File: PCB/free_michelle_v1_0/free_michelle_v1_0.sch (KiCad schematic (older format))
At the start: 100 parts, among them J1 Zworka_TX, J10 ARK, J11 ARK, J12 Zworka_Buzzer, J13 ARK, J14 ARK, J15 Gniazdo 5VP DC 5,5x2,5, J16 Gniazdo 9V DC 5,5x2,5, J2 Zworka_RX, J3 GROVE_SW, J4 ARK, J5 ARK, J6 ARK, J7 ARK, J8 GROVE_SW, J9 A02YYUW_GroveCON, K1 FINDER-36.11, K2 FINDER-36.11, K3 FINDER-36.11, K4 FINDER-36.11, K5 FINDER-36.11, K6 FINDER-36.11, K7 FINDER-36.11, K8 FINDER-36.11, Q1 MMBT4403_PNP, Q2 MMBT4403_PNP, Q3 MMBT4403_PNP, Q4 MMBT4403_PNP, Q5 BSS138, Q6 MMBT4403_PNP, Q7 MMBT4403_PNP, Q8 MMBT4403_PNP, Q9 MMBT4403_PNP, SW1 Rotary_Encoder, SW2 SW_Push, SW3 SW_Push, U1 EEPROM_24AA01, U2 ESP8266_NodeMCU_v2, U3 DS3231M_RTC, U4 NRF24L01_Breakout, U5 BMP280, U6 LD1117V33, U7 L7805, U8 LD1117V33

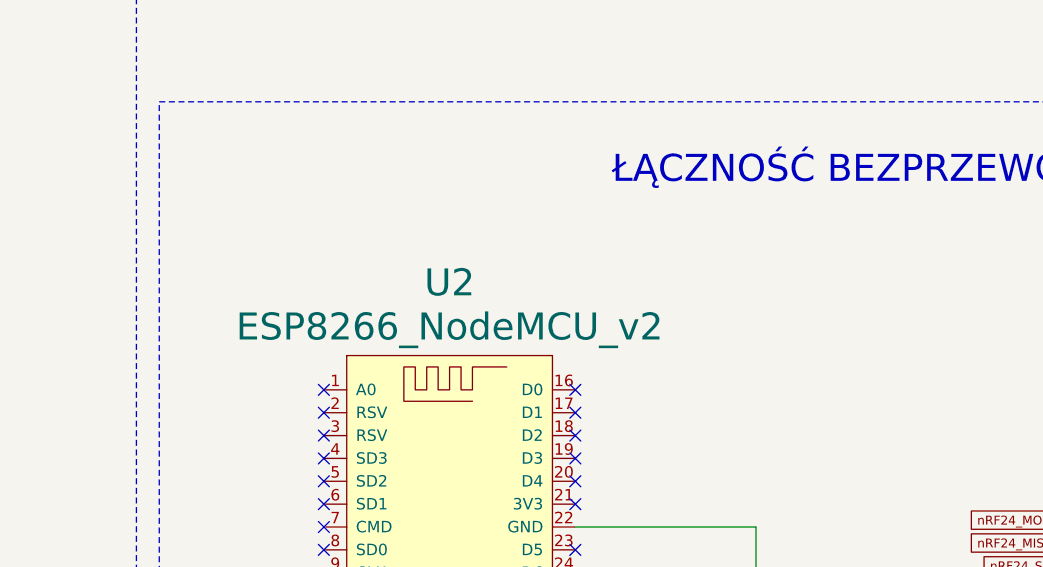
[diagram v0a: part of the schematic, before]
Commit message: Powybierane wszystkie obudowy i poprzypisywane footprinty
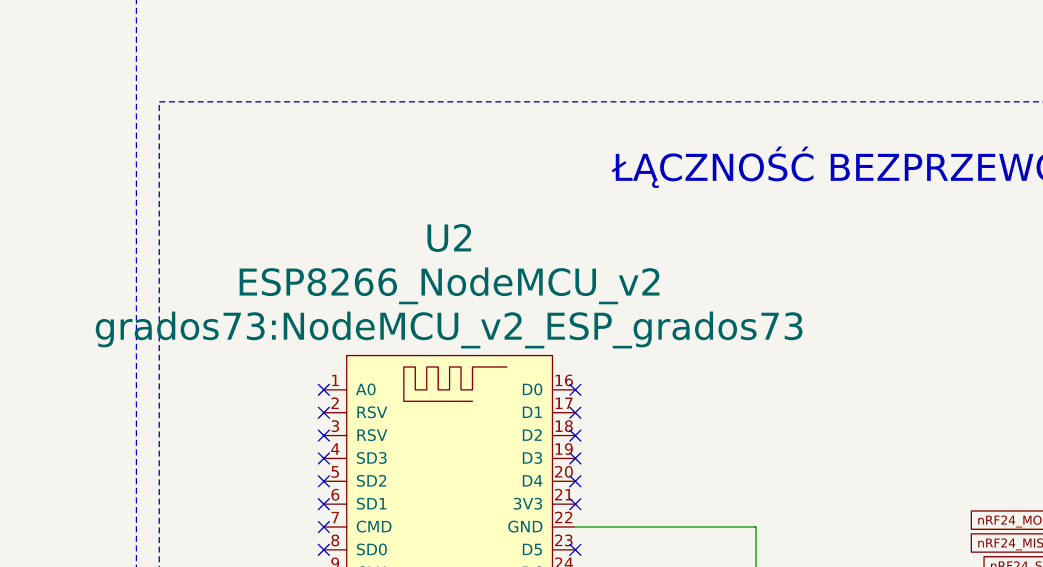
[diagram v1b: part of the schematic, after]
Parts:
- C1, C2, C3, C4, C6, C7, C8: footprint (none) -> Capacitor_SMD:C_1206_3216Metric
- C10, C12, C13, C15, C16, C17: footprint (none) -> Capacitor_THT:C_Disc_D5.0mm_W2.5mm_P5.00mm
- C11, C14, C9: footprint (none) -> Capacitor_THT:CP_Radial_D5.0mm_P2.50mm
- C5: footprint (none) -> Capacitor_THT:C_Disc_D3.0mm_W2.0mm_P2.50mm
- D1: footprint (none) -> grados73:TFT_2_4_c_240x320_SPI
- D10, D3, D4, D5, D6, D7, D8, D9: footprint (none) -> Diode_THT:D_DO-41_SOD81_P10.16mm_Horizontal
- D11: footprint LED_THT:LED_D3.0mm_Clear -> LED_THT:LED_D3.0mm
- D12: footprint (none) -> LED_THT:LED_D3.0mm_Clear
- J10, J11, J13, J14, J4, J5, J6, J7: footprint (none) -> TerminalBlock:TerminalBlock_Altech_AK300-3_P5.00mm
- J15: footprint (none) -> TerminalBlock:TerminalBlock_Altech_AK300-2_P5.00mm
- J16: footprint (none) -> Connector_BarrelJack:BarrelJack_Horizontal
- R1, R10, R11, R12, R13, R14, R15, R16, R17, R18, R19, R2, R3, R4, R5, R6, R7, R9: footprint (none) -> Resistor_SMD:R_1206_3216Metric
- R20, R21, R8: footprint (none) -> Resistor_THT:R_Axial_DIN0207_L6.3mm_D2.5mm_P7.62mm_Horizontal
- U2: footprint (none) -> grados73:NodeMCU_v2_ESP_grados73

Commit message: Ulozone wstepnie elementy na PCB
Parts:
- Term1: footprint Connector_PinHeader_2.00mm:PinHeader_1x04_P2.00mm_Vertical -> Connector_PinHeader_2.00mm:PinHeader_1x04_P2.00mm_Horizontal
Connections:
- net +5VP: now also D12.2 (A), SW3.1; no longer R21.1
- net +9V: now also D11.2 (A), SW2.1; no longer R20.1
- net DS3231_SCL_PB6: no longer R2.1
- net DS3231_SDA_PB9: now also R2.1
- net ESP_TX_RX_STM__U1_PB7: now also J1.2 (Pin_2)
- net GND: now also R20.1, R21.1, U2.22 (GND)
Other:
- note removed: "LOGIKI 3,3V"
- note removed: "LOGIKI 5V"
- note removed: "NAPIĘCIE ZASILANIA 3,3V"
- moved on the sheet: D11, D12, J15, J16, R20, R21, SW2, SW3

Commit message: Poprawki po rozmowie z Mackiem umieszczone na schemacie
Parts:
- removed LED1: WS2812b_ARK, Connector_PinHeader_2.54mm:PinHeader_1x03_P2.54mm_Vertical, symbol Connector:Conn_01x03_Female
- added LED1: WS2812b_GROVE, Connector_PinHeader_2.00mm:PinHeader_1x04_P2.00mm_Horizontal, symbol Connector:Conn_01x04_Male
- added R22: 4K7, Resistor_SMD:R_1206_3216Metric, symbol Device:R_Small
- C7, C8: footprint Capacitor_SMD:C_1206_3216Metric -> Capacitor_THT:C_Disc_D5.0mm_W2.5mm_P2.50mm
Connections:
- net +3V3: now also J3.4 (Pin_4), J8.4 (Pin_4), Term1.4 (Pin_4), R22.1; no longer J3.1 (Pin_1), J8.1 (Pin_1)
- net +5V: no longer C7.1, C8.1, Term1.4 (Pin_4)
- net +5VP: now also C7.1, LED1.4 (Pin_4)
- net +9V: now also C8.1
- net DS18B20_1WIRE_PA15: now also R22.2
- net GND: now also J3.2 (Pin_2), J8.2 (Pin_2), LED1.2 (Pin_2); no longer J3.4 (Pin_4), J8.4 (Pin_4)
- net at TFT_CONTROLLER1.42 (SWCLK): now also J3.1 (Pin_1); no longer J3.3 (Pin_3)
- net at TFT_CONTROLLER1.43 (SWIO): now also J3.3 (Pin_3); no longer J3.2 (Pin_2)
- net at GPIO_CONTROLLER1.42 (SWCLK): now also J8.1 (Pin_1); no longer J8.3 (Pin_3)
- net at GPIO_CONTROLLER1.43 (SWIO): now also J8.3 (Pin_3); no longer J8.2 (Pin_2)
- net at Q5.3 (D), R15.1: now also LED1.3 (Pin_3)
- no-connect marks 56 -> 57

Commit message: Gotowa płytka przed generacją gerberow
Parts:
- removed U6, U8: LD1117V33, Package_TO_SOT_THT:TO-220-3_Vertical, symbol grad73_library:LD1117V33
- added H1, H2, H3, H4: MountingHole, MountingHole:MountingHole_3.2mm_M3, symbol Mechanical:MountingHole
- added U6, U8: LD1117AV33, Package_TO_SOT_THT:TO-220-3_Vertical, symbol Regulator_Linear:LD1117S12TR_SOT223
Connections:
- net +3.3VP: now also U6.2 (VO)
- net +3V3: now also U8.2 (VO)
- net +9V: now also U6.3 (VI), U8.3 (VI)
- net GND: now also U6.1 (GND), U8.1 (GND)
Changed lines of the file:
@@
 	19610 4090 19450 4090
-$Comp
-L grad73_library:LD1117V33 U8
-U 1 1 61E4A9E3
-P 20120 2810
-F 0 "U8" H 20120 3052 50  0000 C CNN
-F 1 "LD1117V33" H 20120 2961 50  0000 C CNN
-F 2 "Package_TO_SOT_THT:TO-220-3_Vertical" H 20145 2660 50  0001 L CIN
-F 3 "" H 20120 2760 50  0001 C CNN
-	1    20120 2810
-	1    0    0    -1
-$EndComp
 $Comp
 L free_michelle_v1_0-rescue:grad73_library_24AA01-free_michelle_v1_0-cache U1
@@
 NoConn ~ 12380 4120
 $Comp
-L grad73_library:LD1117V33 U6
-U 1 1 64E78405
-P 17820 2830
-F 0 "U6" H 17820 3072 50  0000 C CNN
-F 1 "LD1117V33" H 17820 2981 50  0000 C CNN
-F 2 "Package_TO_SOT_THT:TO-220-3_Vertical" H 17845 2680 50  0001 L CIN
-F 3 "" H 17820 2780 50  0001 C CNN
-	1    17820 2830
-	1    0    0    -1
-$EndComp
-$Comp
 L power:+9V #PWR045
 U 1 1 64E7923F
@@
 Wire Wire Line
 	17280 2890 17280 2830
-Connection ~ 17280 2830
-Wire Wire Line
-	17280 2830 17520 2830
 Wire Wire Line
 	17820 3250 18360 3250
@@
 	1    0    0    -1
 $EndComp
+Connection ~ 17280 2830
+Wire Wire Line
+	17280 2830 17520 2830
+$Comp
+L Regulator_Linear:LD1117S12TR_SOT223 U6
+U 1 1 697826F5
+P 17820 2830
+F 0 "U6" H 17820 3072 50  0000 C CNN
+F 1 "LD1117AV33" H 17820 2981 50  0000 C CNN
+F 2 "Package_TO_SOT_THT:TO-220-3_Vertical" H 17820 3030 50  0001 C CNN
+F 3 "https://www.tme.eu/Document/bad00e7fc591b73ff810af309b2bb7a4/LD1117A.pdf" H 17920 2580 50  0001 C CNN
+	1    17820 2830
+	1    0    0    -1
+$EndComp
+$Comp
+L Regulator_Linear:LD1117S12TR_SOT223 U8
+U 1 1 697DB078
+P 20120 2810
+F 0 "U8" H 20120 3052 50  0000 C CNN
+F 1 "LD1117AV33" H 20120 2961 50  0000 C CNN
+F 2 "Package_TO_SOT_THT:TO-220-3_Vertical" H 20120 3010 50  0001 C CNN
+F 3 "https://www.tme.eu/Document/bad00e7fc591b73ff810af309b2bb7a4/LD1117A.pdf" H 20220 2560 50  0001 C CNN
+	1    20120 2810
+	1    0    0    -1
+$EndComp
+$Comp
+L Mechanical:MountingHole H1
+U 1 1 61EC6BA5
+P 17500 6660
+F 0 "H1" H 17600 6706 50  0000 L CNN
+F 1 "MountingHole" H 17600 6615 50  0000 L CNN
+F 2 "MountingHole:MountingHole_3.2mm_M3" H 17500 6660 50  0001 C CNN
+F 3 "~" H 17500 6660 50  0001 C CNN
+	1    17500 6660
+	1    0    0    -1
+$EndComp
+$Comp
+L Mechanical:MountingHole H2
+U 1 1 61EC80BA
+P 18260 6660
+F 0 "H2" H 18360 6706 50  0000 L CNN
+F 1 "MountingHole" H 18360 6615 50  0000 L CNN
+F 2 "MountingHole:MountingHole_3.2mm_M3" H 18260 6660 50  0001 C CNN
+F 3 "~" H 18260 6660 50  0001 C CNN
+	1    18260 6660
+	1    0    0    -1
+$EndComp
+$Comp
+L Mechanical:MountingHole H3
+U 1 1 61EC8464
+P 19210 6660
+F 0 "H3" H 19310 6706 50  0000 L CNN
+F 1 "MountingHole" H 19310 6615 50  0000 L CNN
+F 2 "MountingHole:MountingHole_3.2mm_M3" H 19210 6660 50  0001 C CNN
+F 3 "~" H 19210 6660 50  0001 C CNN
+	1    19210 6660
+	1    0    0    -1
+$EndComp
+$Comp
+L Mechanical:MountingHole H4
+U 1 1 61EC8838
+P 20120 6660
+F 0 "H4" H 20220 6706 50  0000 L CNN
+F 1 "MountingHole" H 20220 6615 50  0000 L CNN
+F 2 "MountingHole:MountingHole_3.2mm_M3" H 20120 6660 50  0001 C CNN
+F 3 "~" H 20120 6660 50  0001 C CNN
+	1    20120 6660
+	1    0    0    -1
+$EndComp
